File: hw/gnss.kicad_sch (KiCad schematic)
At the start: 23 parts, among them J3 U.FL GNSS, U6 TLV75533PDBVR, U7 L76KB-A58

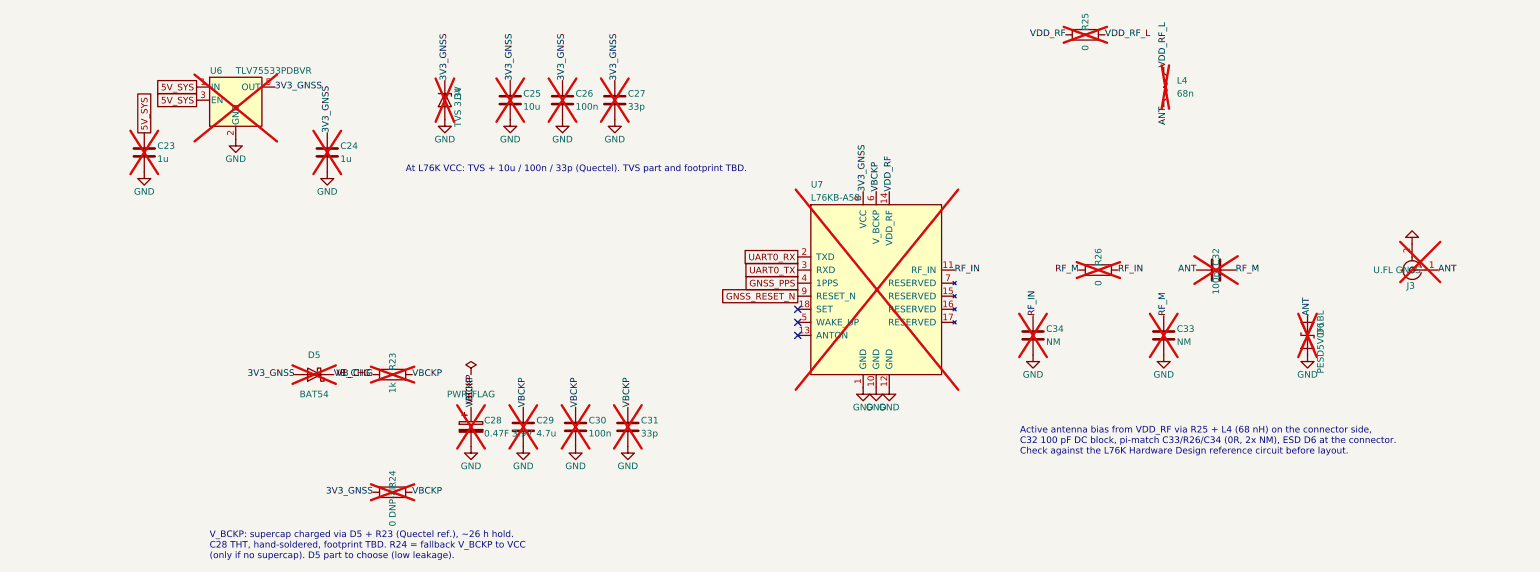
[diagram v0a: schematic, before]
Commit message: hw: draw schematic with wires instead of net labels
Connections inside a sheet are now wires; global labels remain only for
nets that cross sheets, GND stays on power symbols. Pico pins 9-20 are
fanned out so the 33R series resistors fit in one column, and the
SX1302_RESET pull-down moves to the LoRa sheet. Netlist unchanged, ERC
clean. Project file now carries KiCad's default settings.

Co-Authored-By: Claude Opus 5.5 <noreply@anthropic.com>
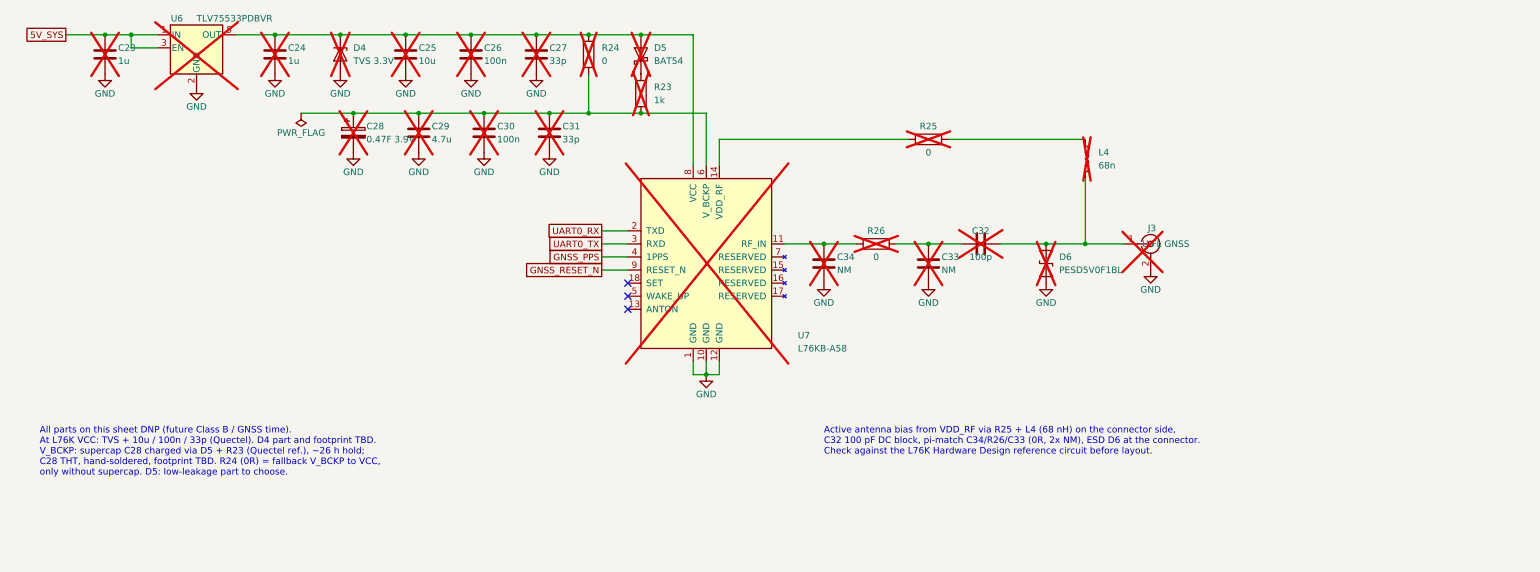
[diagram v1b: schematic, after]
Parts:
- R24: value 0 DNP-alt -> 0
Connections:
- net 3V3_GNSS: no longer names the net of C24.1, C25.1, C26.1, C27.1, D4.1 (K), D5.2 (A), R24.1, U6.5 (OUT), U7.8 (VCC)
- net ANT: no longer names the net of D6.2 (A2), J3.1 (In), L4.2
- net ANT: now also C32.2; no longer C32.1
- net RF_IN: no longer names the net of C34.1, U7.11 (RF_IN)
- net RF_IN: now also R26.1; no longer R26.2
- removed net RF_M: C32.2, C33.1, R26.1
- net VBCKP: no longer names the net of C28.1, C29.1, C30.1, C31.1, R23.2, R24.2, U7.6 (V_BCKP)
- net VB_CHG: no longer names the net of D5.1 (K), R23.1
- net VDD_RF: no longer names the net of R25.1, U7.14 (VDD_RF)
- net VDD_RF_L: no longer names the net of L4.1, R25.2
- new net: C32.1, C33.1, R26.2
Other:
- note added: "Active antenna bias from VDD_RF via R25 + L4 (68 nH) on the connector side, C32 100 pF DC block, pi-match C34/R26/C33 (0R, 2x NM), ESD D6 at the connector. Check against the L76K Hardware Design reference circuit before layout."
- note added: "All parts on this sheet DNP (future Class B / GNSS time). At L76K VCC: TVS + 10u / 100n / 33p (Quectel). D4 part and footprint TBD. V_BCKP: supercap C28 charged via D5 + R23 (Quectel ref.), ~26 h hold; C28 THT, hand-soldered, footprint TBD. R24 (0R) = fallback V_BCKP to VCC, only without supercap. D5: low-leakage part to choose."
- note removed: "Active antenna bias from VDD_RF via R25 + L4 (68 nH) on the connector side, C32 100 pF DC block, pi-match C33/R26/C34 (0R, 2x NM), ESD D6 at the connector. Check against the L76K Hardware Design reference circuit before layout."
- note removed: "At L76K VCC: TVS + 10u / 100n / 33p (Quectel). TVS part and footprint TBD."
- note removed: "V_BCKP: supercap charged via D5 + R23 (Quectel ref.), ~26 h hold. C28 THT, hand-soldered, footprint TBD. R24 = fallback V_BCKP to VCC (only if no supercap). D5 part to choose (low leakage)."
- moved on the sheet: C23, C24, C25, C26, C27, C28, C29, C30, C31, C32, C33, C34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
